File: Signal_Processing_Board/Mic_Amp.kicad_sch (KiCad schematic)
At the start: 7 parts, among them U1 INA128

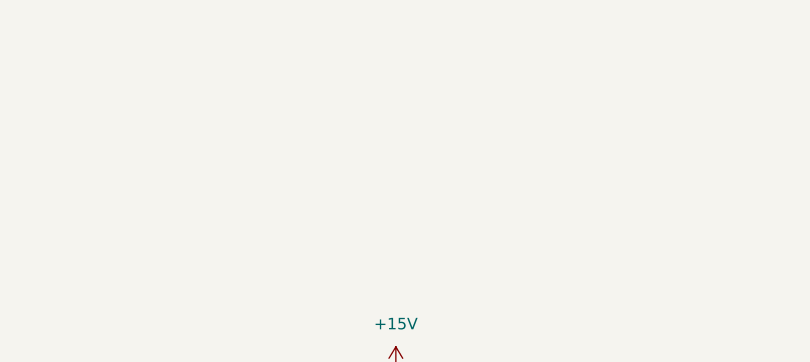
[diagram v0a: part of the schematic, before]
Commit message: Updated file structure and added PDF of schematic
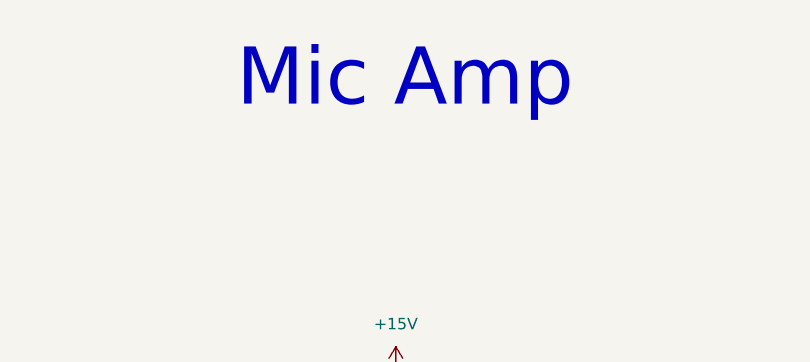
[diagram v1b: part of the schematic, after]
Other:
- note added: "Mic Amp"
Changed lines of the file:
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@@
+		)
+	)
+	(text "Mic Amp"
+		(exclude_from_sim no)
+		(at 133.096 31.242 0)
+		(effects
+			(font
+				(size 6.35 6.35)
+			)
 		)
 	)
